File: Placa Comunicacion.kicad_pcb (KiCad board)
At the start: 2 copper layers, 141.6 x 91.6 mm, 98 parts, among them J1 Screw_Terminal_01x02, J2 ARJM11C7-009-AB-EW2, J3 Screw_Terminal_01x04, J42 DE9_Receptacle_MountingHoles, J45 USB_A_Female_P2.5mm, Q1 BSS123, Q2 Si2319CDS, U1 HC-05, U11 USBLC6-2SC6, U14 MAX232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

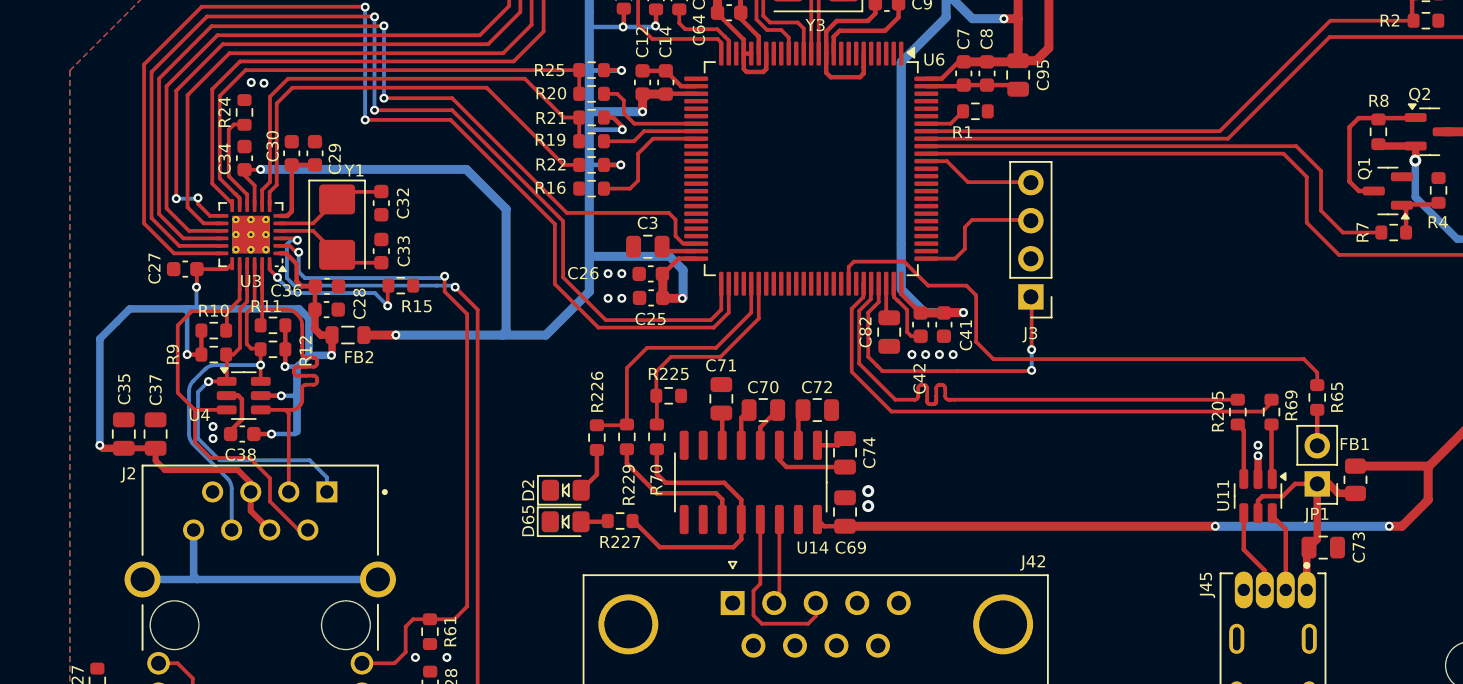
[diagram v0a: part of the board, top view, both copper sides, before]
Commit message: Se estandariza algunos atributos: valores, librerias. Se actualiza pcb y se guarda.
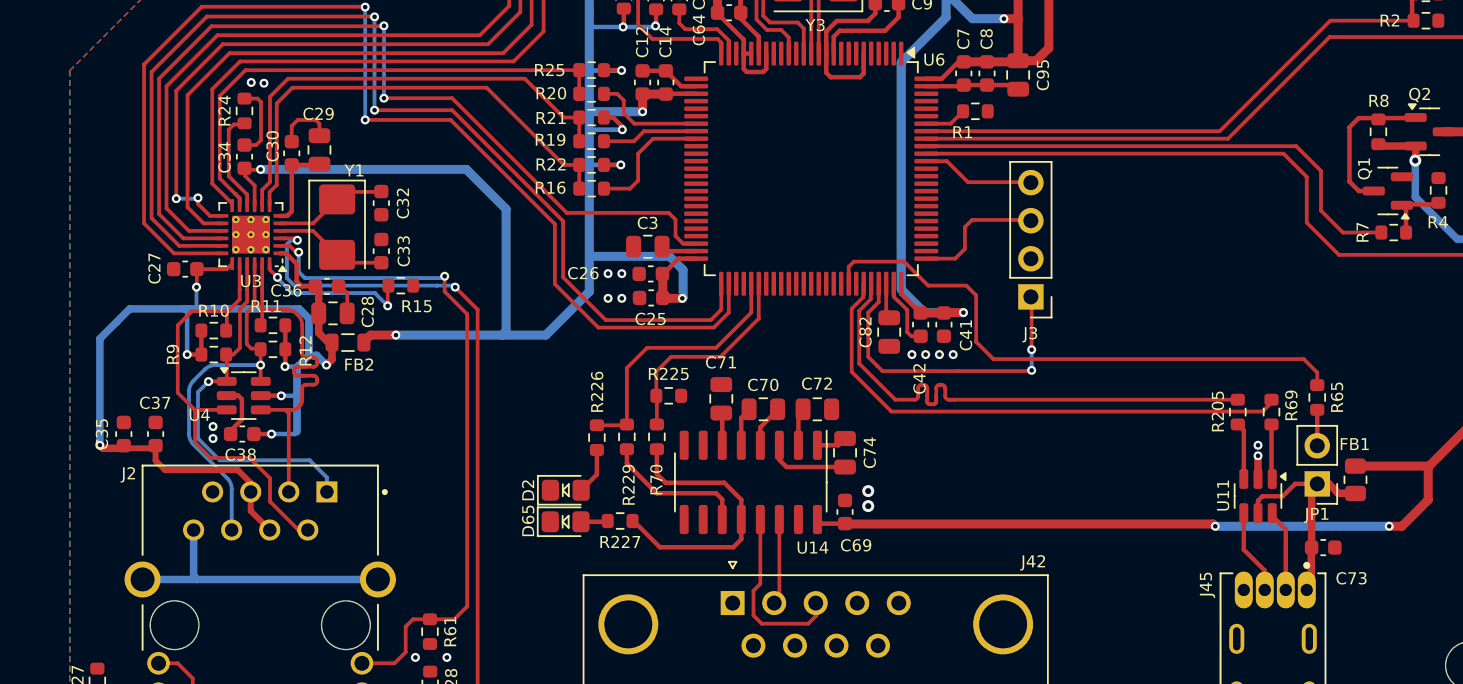
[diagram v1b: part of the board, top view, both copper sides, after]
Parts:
- C1, C34, C38: value 100nF 50V -> 100nF/50V
- C28: footprint 1-Capacitor:C_0603_1608Metric -> Capacitor_SMD:C_0805_2012Metric
- C29: value 1uF 16V -> 1uF/50V; footprint 1-Capacitor:C_0603_1608Metric -> Capacitor_SMD:C_0805_2012Metric
- C35, C37, C69, C73: value 100nF 50V -> 100nF/50V; footprint 1-Capacitor:C_0805_2012Metric -> 1-Capacitor:C_0603_1608Metric
- C39: value 47uF 25V -> 47uF/25V
- C4, C6: value 30pF 50V -> 30pF/50V
- C40: value 4.7uF 25V -> 4u7F/25V
- C70, C71, C72, C74: value 1uF 50V -> 1uF/50V; footprint 1-Capacitor:C_0805_2012Metric -> Capacitor_SMD:C_0805_2012Metric
- R26: value 1k5 -> 1k
- moved FB2 0.50 mm to (84.2, 133.4)
- moved C28 0.49 mm to (83.2, 131.5)
- moved C29 0.38 mm to (82.2, 120.6)
- moved C34 0.10 mm to (77.2, 121.0)
- moved R24 0.10 mm to (77.2, 118.0)
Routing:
- net GND: track 44.8 -> 55.9 mm
- net Net-(U3-RXD1/MODE1): track 29.8 -> 31.3 mm

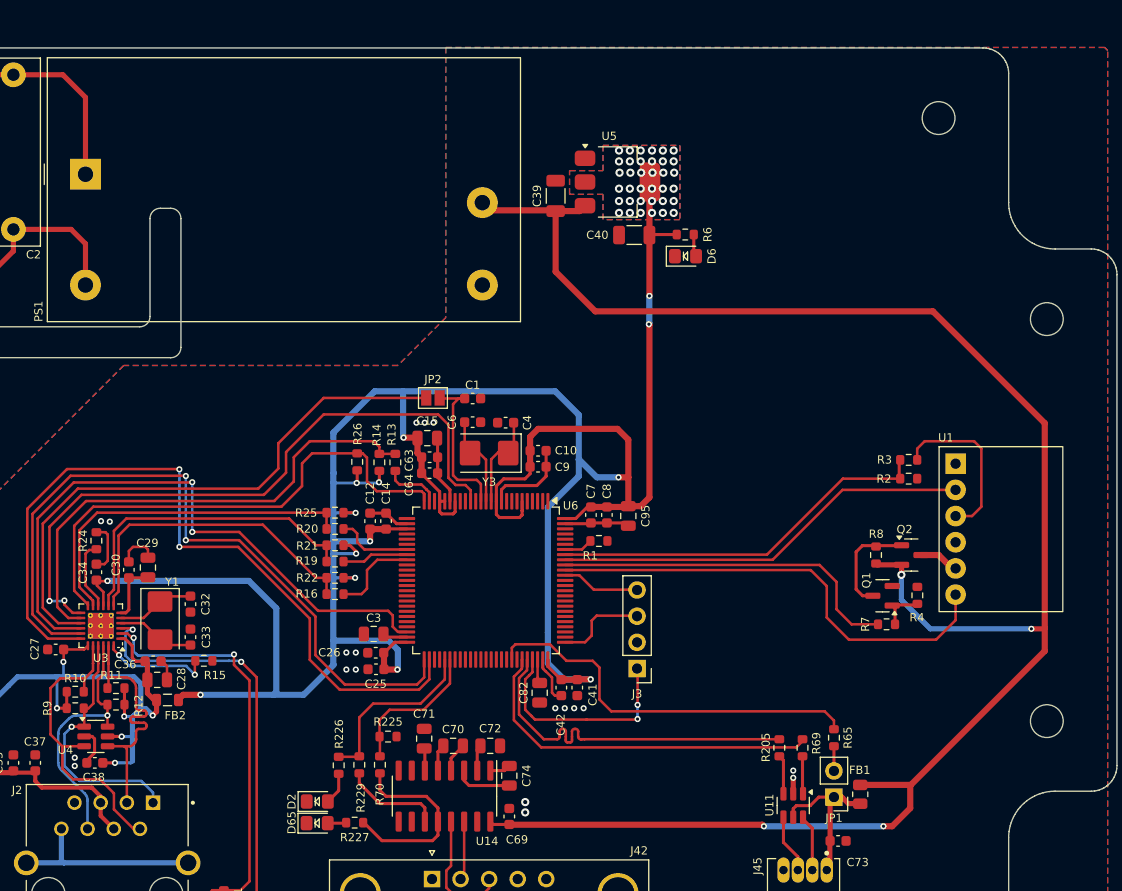
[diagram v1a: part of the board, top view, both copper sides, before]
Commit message: Se estandariza losc omponentes, se cambian algunos valores para evitar gastos adicionales. Se termina y comprueb el part list para jlcpcb
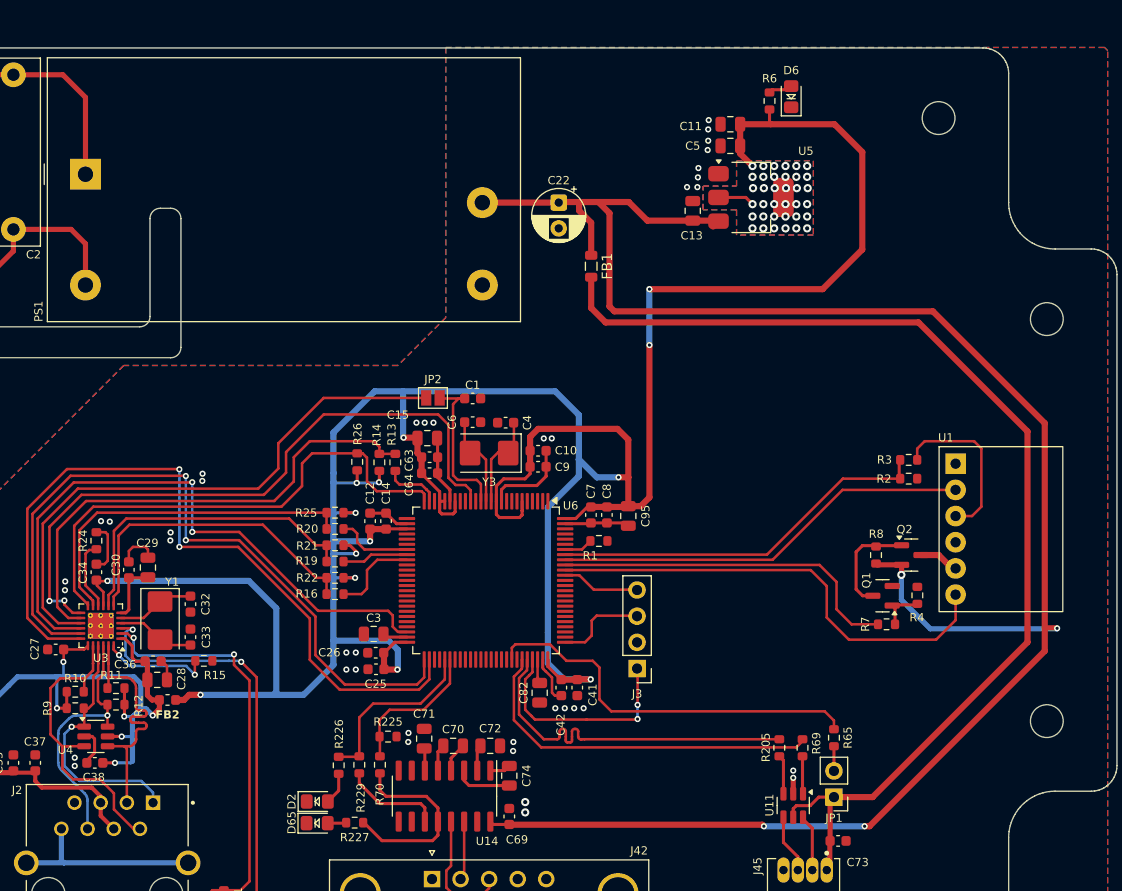
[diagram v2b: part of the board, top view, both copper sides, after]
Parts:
- removed C39: 47uF/25V, 1-Capacitor:C_1206_3216Metric
- removed C40: 4u7F/25V, 1-Capacitor:C_1206_3216Metric
- added C11: 2u2F/50V, Capacitor_SMD:C_0805_2012Metric, F.Cu at (138.8, 77.6)
- added C13: 2u2F/50V, Capacitor_SMD:C_0805_2012Metric, F.Cu at (135.1, 86.0)
- added C22: 47uF/25V, Capacitor_THT:CP_Radial_D5.0mm_P2.50mm, F.Cu at (122.1, 85.2)
- added C5: 2u2F/50V, Capacitor_SMD:C_0805_2012Metric, F.Cu at (138.8, 79.7)
- FB1: value 220R -> 100mR/1A; footprint 1-Resistor:R_0805_2012Metric -> Inductor_SMD:L_0805_2012Metric
- FB2: value 600R -> 450mR/200mA; footprint Inductor_SMD:L_0805_2012Metric -> Inductor_SMD:L_0603_1608Metric
- R225: value 2k -> 20k
- R226, R227, R70: value 1k -> 10k
- R27, R28: value 510R -> 10k
- R6: value 680R -> 10k
- moved FB1 57.5 mm to (125.2, 91.4)
- moved D6 18.6 mm to (144.7, 74.9), turned to 90 degrees
- moved R6 15.3 mm to (142.6, 75.3), turned to 90 degrees
- moved U5 13.0 mm to (140.8, 84.7)
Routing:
- net Vbus: track 15.4 -> 109.1 mm
- net +3.3V: track 266.4 -> 307.6 mm
- net +5V: track 180.5 -> 195.4 mm
- net /Ethernet/VDD_LAN_F_3V3: track 76.5 -> 77.0 mm
- net GND: vias 21 -> 41

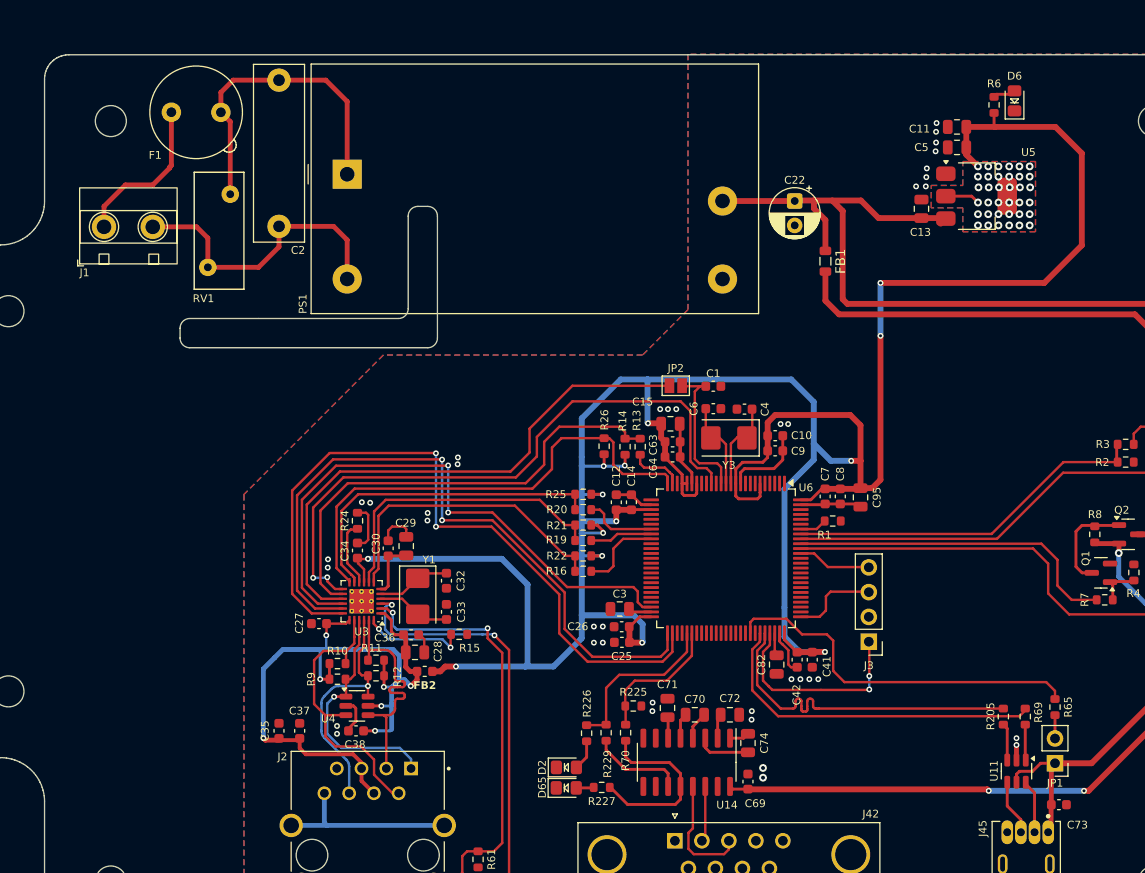
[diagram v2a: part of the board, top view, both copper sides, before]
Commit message: Se añade led status y eeprom externa. Se actutliza y añade serigrafía a la pcb, se escoge uC de menos flash debido a la escasez del uC planeado, sin embargo, funcionará a recomendacion del programador. Se revisa en jlcpcb y se espera su envío
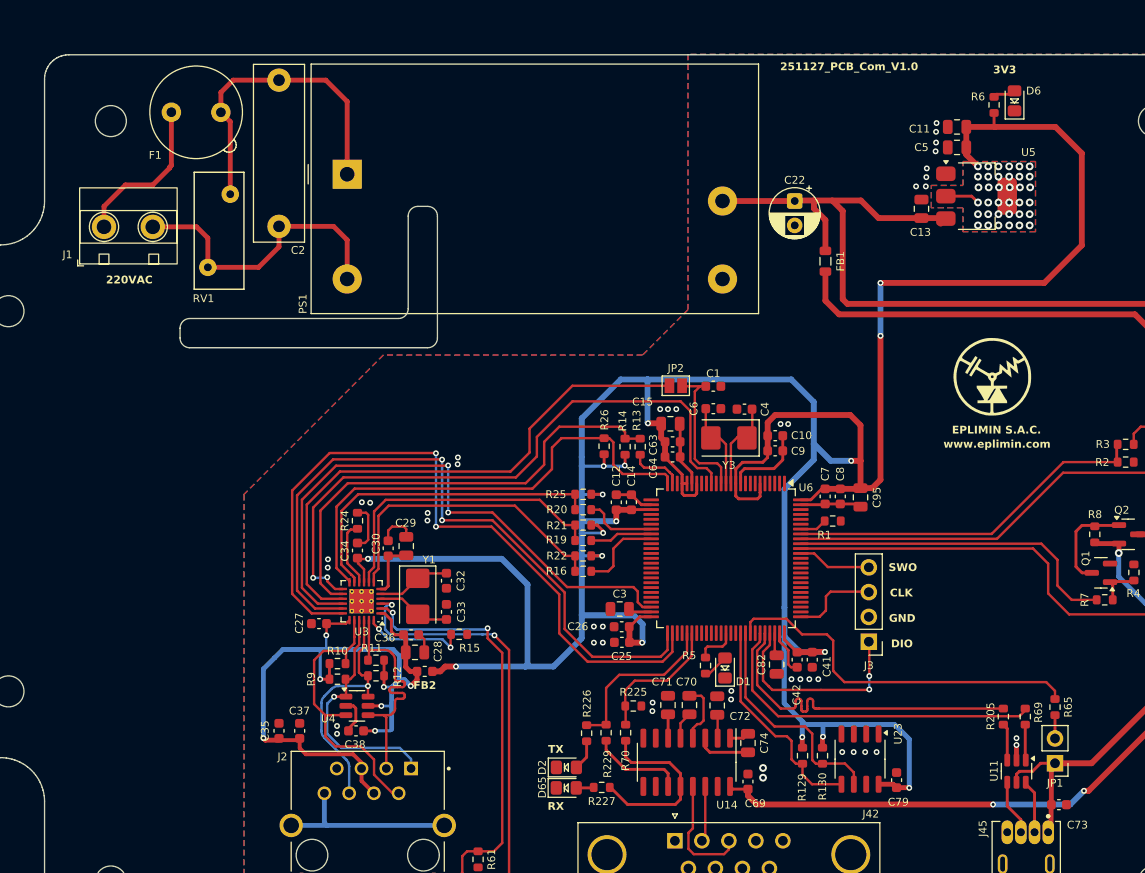
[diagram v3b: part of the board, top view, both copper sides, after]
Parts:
- added C79: 100nF/50V, 1-Capacitor:C_0603_1608Metric, F.Cu at (132.6, 144.6)
- added D1: RED, 1-Led:LED_0805, F.Cu at (115.0, 133.1)
- added G1: LOGO, LOGO, F.Cu at (142.3, 103.2)
- added R129: 2k2, Resistor_SMD:R_0603_1608Metric, F.Cu at (122.9, 142.1)
- added R130: 2k2, Resistor_SMD:R_0603_1608Metric, F.Cu at (125.0, 142.1)
- added R5: 2k2, Resistor_SMD:R_0603_1608Metric, F.Cu at (113.0, 132.8)
- added U23: 24xx256, Package_SO:SO-8_3.9x4.9mm_P1.27mm, F.Cu at (128.8, 142.4)
- moved C72 1.61 mm to (114.2, 136.9), turned to 90 degrees
- moved C70 1.14 mm to (111.3, 136.9), turned to -90 degrees
- moved C71 0.30 mm to (109.1, 136.9)
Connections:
- net ETH_nRST renamed /ETH_nRST
- U6 pad 63: unconnected-(U6-PC6-Pad63) -> /LED_STATUS
- U6 pad 66: unconnected-(U6-PC9-Pad66) -> /MCU_I2C3_SDA
- U6 pad 67: unconnected-(U6-PA8-Pad67) -> /MCU_I2C3_SCL
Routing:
- net +3.3V: track 307.6 -> 342.3 mm, vias 50 -> 53
- net /MCU_I2C3_SCL: track 0.00 -> 23.7 mm
- net /MCU_I2C3_SDA: track 0.00 -> 22.6 mm
- net /LED_STATUS: track 0.00 -> 4.28 mm
- net Net-(U14-C2+): track 2.88 -> 6.28 mm
- net Net-(D1-A): track 0.00 -> 2.66 mm
- net +5V: track 195.4 -> 197.0 mm
- net GND: vias 41 -> 45
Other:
- board text added: "220VAC"
- board text added: "251127_PCB_Com_V1.0"
- board text added: "3V3"
- board text added: "CLK"
- board text added: "DIO"
- board text added: "EPLIMIN S.A.C."
- board text added: "GND"
- board text added: "RX"
- board text added: "SWO"
- board text added: "TX"
- board text added: "www.eplimin.com"
